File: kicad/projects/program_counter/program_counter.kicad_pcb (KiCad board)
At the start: 2 copper layers, 0 parts

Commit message: Program counter complete.
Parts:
- added C1: 0.1uF, Capacitor_THT:C_Disc_D5.0mm_W2.5mm_P5.00mm, F.Cu at (208.3, 82.8)
- added C10: 33uF, Capacitor_THT:CP_Radial_D6.3mm_P2.50mm, F.Cu at (66.0, 134.6)
- added C11: 33uF, Capacitor_THT:CP_Radial_D6.3mm_P2.50mm, F.Cu at (172.7, 116.8)
- added C12: 33uF, Capacitor_THT:CP_Radial_D6.3mm_P2.50mm, F.Cu at (152.4, 73.7)
- added C2: 0.1uF, Capacitor_THT:C_Disc_D5.0mm_W2.5mm_P5.00mm, F.Cu at (182.9, 111.8)
- added C3: 0.1uF, Capacitor_THT:C_Disc_D5.0mm_W2.5mm_P5.00mm, F.Cu at (142.2, 116.8)
- added C4: 0.1uF, Capacitor_THT:C_Disc_D5.0mm_W2.5mm_P5.00mm, F.Cu at (215.9, 111.8)
- added C5: 0.1uF, Capacitor_THT:C_Disc_D5.0mm_W2.5mm_P5.00mm, F.Cu at (114.3, 116.8)
- added C6: 0.1uF, Capacitor_THT:C_Disc_D5.0mm_W2.5mm_P5.00mm, F.Cu at (160.0, 82.8)
- added C7: 0.1uF, Capacitor_THT:C_Disc_D5.0mm_W2.5mm_P5.00mm, F.Cu at (86.4, 116.8)
- added C8: 0.1uF, Capacitor_THT:C_Disc_D5.0mm_W2.5mm_P5.00mm, F.Cu at (58.4, 116.8)
- added C9: 0.1uF, Capacitor_THT:C_Disc_D5.0mm_W2.5mm_P5.00mm, F.Cu at (124.5, 86.4)
- added D1: LED, eight-bit-computer:LED_D5.0mm_Horizontal_O3.81mm_Z3.0mm, F.Cu at (251.5, 63.5)
- added D10: LED, eight-bit-computer:LED_D5.0mm_Horizontal_O3.81mm_Z3.0mm, F.Cu at (194.3, 63.5)
- added D11: LED, eight-bit-computer:LED_D5.0mm_Horizontal_O3.81mm_Z3.0mm, F.Cu at (188.0, 63.5)
- added D12: LED, eight-bit-computer:LED_D5.0mm_Horizontal_O3.81mm_Z3.0mm, F.Cu at (181.6, 63.5)
- added D13: LED, eight-bit-computer:LED_D5.0mm_Horizontal_O3.81mm_Z3.0mm, F.Cu at (175.3, 63.5)
- added D14: LED, eight-bit-computer:LED_D5.0mm_Horizontal_O3.81mm_Z3.0mm, F.Cu at (168.9, 63.5)
- added D15: LED, eight-bit-computer:LED_D5.0mm_Horizontal_O3.81mm_Z3.0mm, F.Cu at (162.6, 63.5)
- added D16: LED, eight-bit-computer:LED_D5.0mm_Horizontal_O3.81mm_Z3.0mm, F.Cu at (156.2, 63.5)
- added D2: LED, eight-bit-computer:LED_D5.0mm_Horizontal_O3.81mm_Z3.0mm, F.Cu at (245.1, 63.5)
- added D3: LED, eight-bit-computer:LED_D5.0mm_Horizontal_O3.81mm_Z3.0mm, F.Cu at (238.8, 63.5)
- added D4: LED, eight-bit-computer:LED_D5.0mm_Horizontal_O3.81mm_Z3.0mm, F.Cu at (232.4, 63.5)
- added D5: LED, eight-bit-computer:LED_D5.0mm_Horizontal_O3.81mm_Z3.0mm, F.Cu at (226.1, 63.5)
- added D6: LED, eight-bit-computer:LED_D5.0mm_Horizontal_O3.81mm_Z3.0mm, F.Cu at (219.7, 63.5)
- added D7: LED, eight-bit-computer:LED_D5.0mm_Horizontal_O3.81mm_Z3.0mm, F.Cu at (213.4, 63.5)
- added D8: LED, eight-bit-computer:LED_D5.0mm_Horizontal_O3.81mm_Z3.0mm, F.Cu at (207.0, 63.5)
- added D9: LED, eight-bit-computer:LED_D5.0mm_Horizontal_O3.81mm_Z3.0mm, F.Cu at (200.7, 63.5)
- added J1: Conn_01x16_Female, Connector_PinSocket_2.54mm:PinSocket_1x16_P2.54mm_Horizontal, F.Cu at (91.4, 61.0)
- added J2: Control_signal_backplane, eight-bit-computer:backplane-connector-single-row-annotated, F.Cu at (251.5, 144.8)
- added J3: Bus_connection, eight-bit-computer:bus-connection, F.Cu at (147.3, 144.8)
- added J4: Aux_connection, eight-bit-computer:aux-connection, F.Cu at (96.5, 144.8)
- added RN1: R_Network08_US, Resistor_THT:R_Array_SIP9, F.Cu at (215.9, 73.7)
- added RN2: R_Network08_US, Resistor_THT:R_Array_SIP9, F.Cu at (167.6, 73.7)
- added U1: 74HCT04, Package_DIP:DIP-14_W7.62mm, F.Cu at (129.5, 88.9)
- added U2: 74HCT245, Package_DIP:DIP-20_W7.62mm, F.Cu at (213.4, 88.9)
- added U3: 74HCT161, Package_DIP:DIP-16_W7.62mm, F.Cu at (147.3, 119.4)
- added U4: 74HCT245, Package_DIP:DIP-20_W7.62mm, F.Cu at (188.0, 119.4)
- added U5: 74HCT161, Package_DIP:DIP-16_W7.62mm, F.Cu at (119.4, 119.4)
- added U6: 74HCT245, Package_DIP:DIP-20_W7.62mm, F.Cu at (221.0, 119.4)
- added U7: 74HCT161, Package_DIP:DIP-16_W7.62mm, F.Cu at (91.4, 119.4)
- added U8: 74HCT245, Package_DIP:DIP-20_W7.62mm, F.Cu at (165.1, 88.9)
- added U9: 74HCT161, Package_DIP:DIP-16_W7.62mm, F.Cu at (63.5, 119.4)
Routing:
- net VCC: track 0.00 -> 550.0 mm, vias 0 -> 26
- net /PC_IN: track 0.00 -> 235.1 mm
- net /CTNT_01: track 0.00 -> 227.2 mm, vias 0 -> 8
- net /CTNT_02: track 0.00 -> 227.2 mm, vias 0 -> 8
- net /CTNT_03: track 0.00 -> 227.2 mm, vias 0 -> 8
- net /CTNT_00: track 0.00 -> 227.0 mm, vias 0 -> 6
- net /CTNT_07: track 0.00 -> 226.8 mm, vias 0 -> 6
- net /CTNT_06: track 0.00 -> 226.1 mm, vias 0 -> 8
- net /CTNT_05: track 0.00 -> 226.1 mm, vias 0 -> 8
- net /CTNT_04: track 0.00 -> 226.1 mm, vias 0 -> 8
- net /PC_OUT: track 0.00 -> 224.4 mm
- net /CTNT_15: track 0.00 -> 214.7 mm, vias 0 -> 4
- net /CTNT_14: track 0.00 -> 213.9 mm, vias 0 -> 8
- net /CTNT_13: track 0.00 -> 213.9 mm, vias 0 -> 8
- net /CTNT_12: track 0.00 -> 213.9 mm, vias 0 -> 8
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- added copper zone on B.Cu, net GND
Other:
- board outline added: 203.2 x 97.8 mm
- board text added: "Content"
- board text added: "PROGRAM COUNTER"

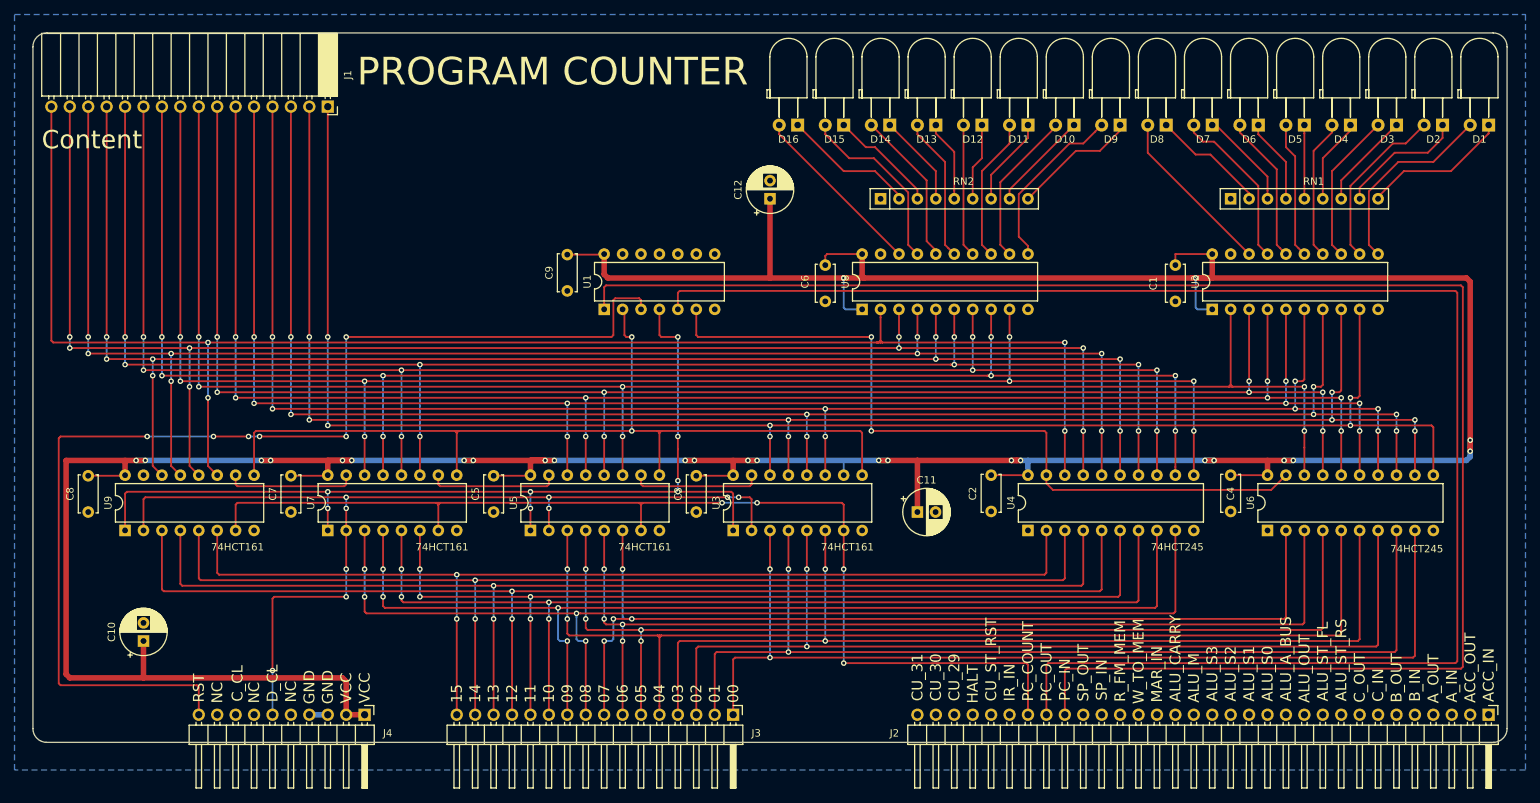
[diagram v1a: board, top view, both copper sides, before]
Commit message: Align output drivers for better PCB layout
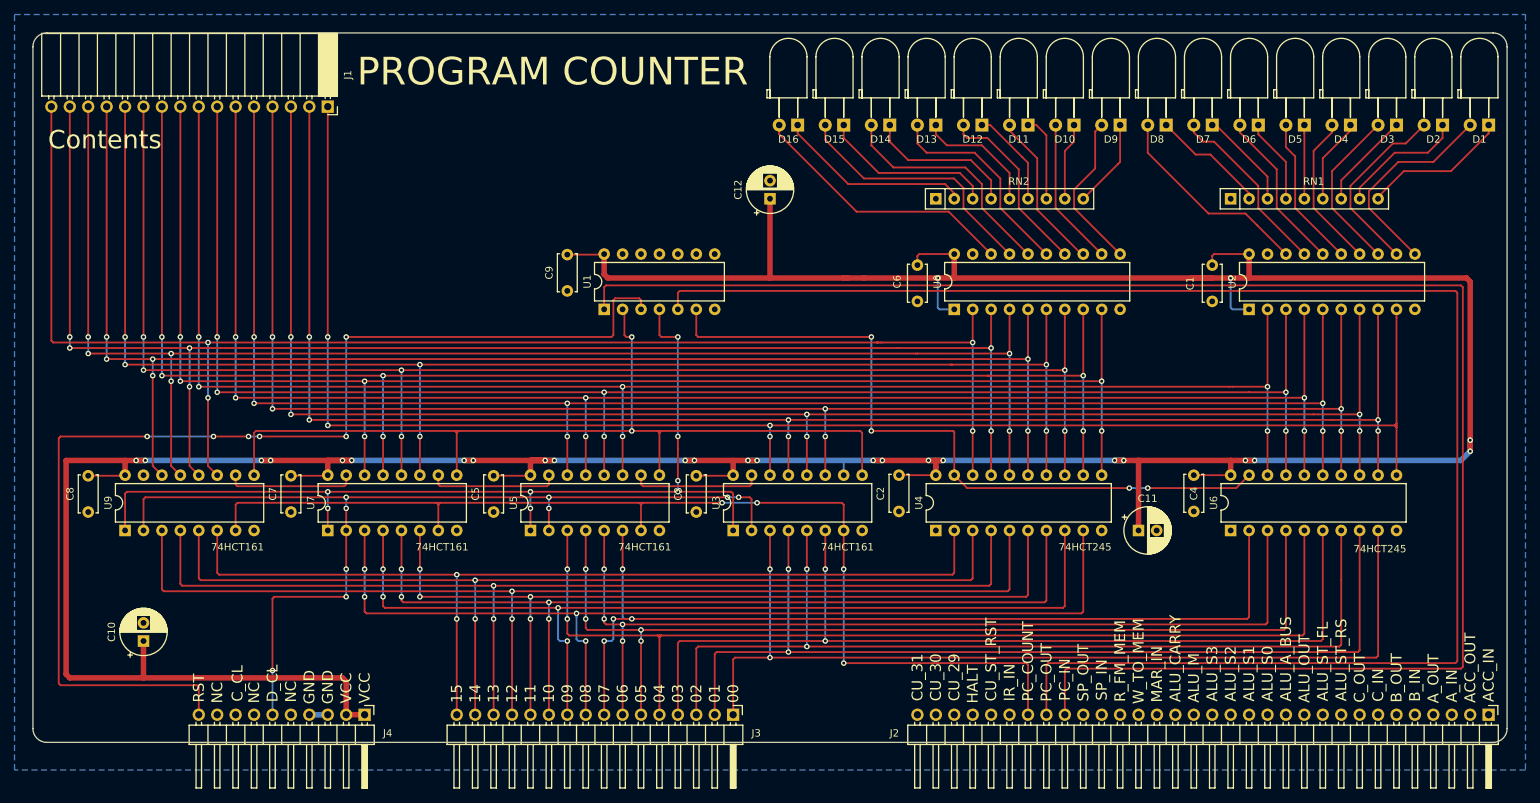
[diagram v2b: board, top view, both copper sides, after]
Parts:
- moved C11 30.6 mm to (203.2, 119.4)
- moved U4 12.7 mm to (175.3, 119.4)
- moved U8 12.7 mm to (177.8, 88.9)
- moved C2 12.7 mm to (170.2, 111.8)
- moved C6 12.7 mm to (172.7, 82.8)
- moved RN2 7.62 mm to (175.3, 73.7)
- moved C1 5.08 mm to (213.4, 82.8)
- moved C4 5.08 mm to (210.8, 111.8)
- moved U2 5.08 mm to (218.4, 88.9)
- moved U6 5.08 mm to (215.9, 119.4)
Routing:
- net /CTNT_15: track 214.7 -> 201.3 mm
- net /CTNT_10: track 213.4 -> 200.7 mm, vias 8 -> 6
- net /BUS_12: track 163.0 -> 150.3 mm
- net /CTNT_14: track 213.9 -> 201.2 mm, vias 8 -> 6
- net /CTNT_13: track 213.9 -> 201.2 mm, vias 8 -> 6
- net /CTNT_12: track 213.9 -> 201.2 mm, vias 8 -> 6
- net /CTNT_09: track 213.6 -> 200.9 mm, vias 8 -> 6
- net /BUS_11: track 130.9 -> 118.2 mm
- net /BUS_10: track 136.6 -> 123.9 mm
- net Net-(D16-Pad2): track 24.6 -> 37.3 mm
- net /CTNT_11: track 213.6 -> 200.9 mm, vias 8 -> 6
- net /CTNT_08: track 213.4 -> 200.7 mm, vias 8 -> 6
- net /BUS_15: track 145.5 -> 132.8 mm
- net /BUS_14: track 151.6 -> 138.9 mm
- net /BUS_13: track 157.2 -> 144.5 mm
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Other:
- board text added: "Contents"
- board text removed: "Content"

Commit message: Move kikad libs to sixteen bit location and update projects.
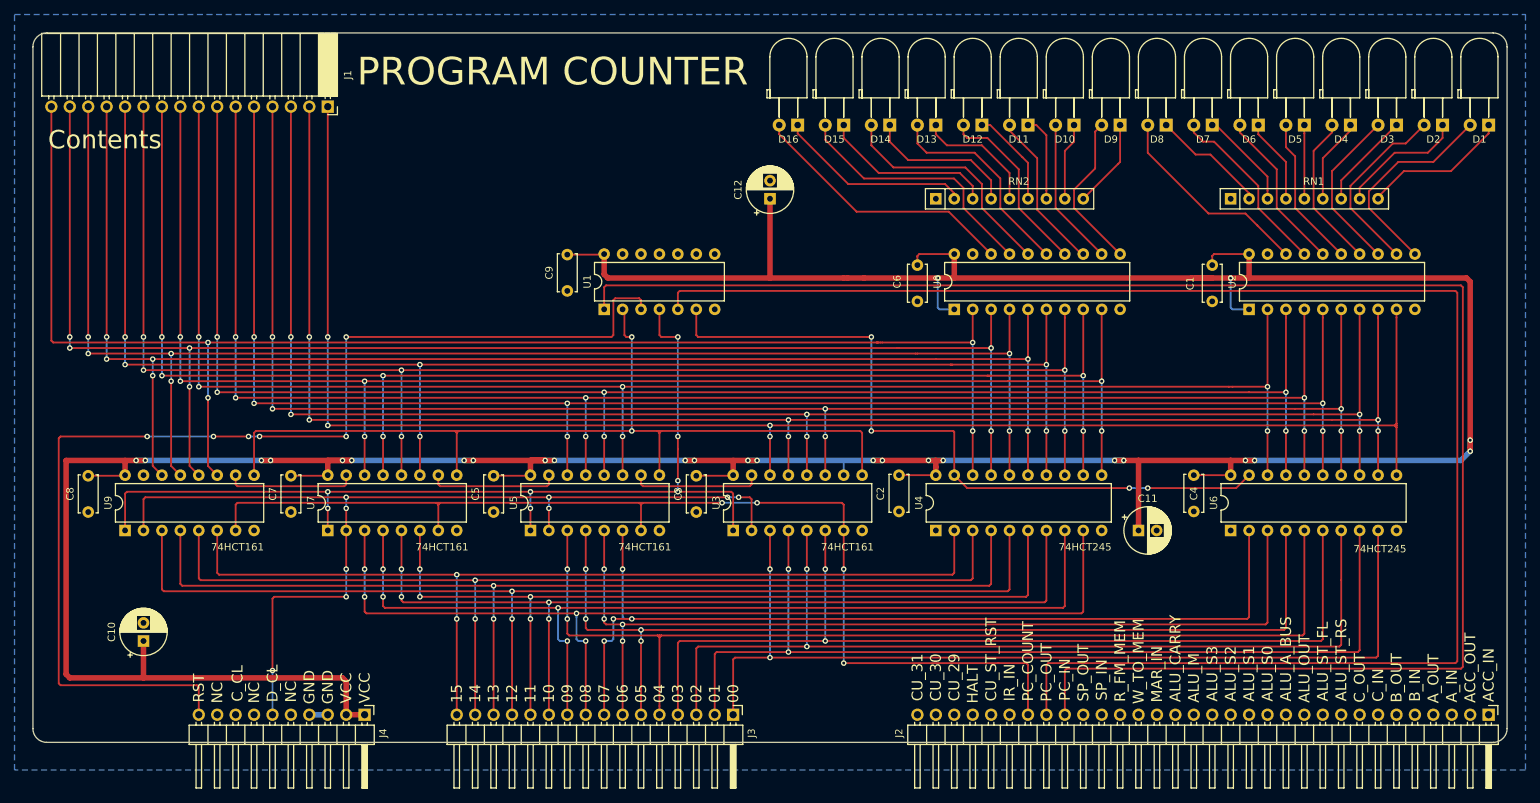
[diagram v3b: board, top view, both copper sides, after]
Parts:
- D1, D10, D11, D12, D13, D14, D15, D16, D2, D3, D4, D5, D6, D7, D8, D9: footprint eight-bit-computer:LED_D5.0mm_Horizontal_O3.81mm_Z3.0mm -> sixteen-bit-computer:LED_D5.0mm_Horizontal_O3.81mm_Z3.0mm
- J2: footprint eight-bit-computer:backplane-connector-single-row-annotated -> sixteen-bit-computer:backplane-connector-single-row-annotated
- J3: footprint eight-bit-computer:bus-connection -> sixteen-bit-computer:bus-connection
- J4: footprint eight-bit-computer:aux-connection -> sixteen-bit-computer:aux-connection

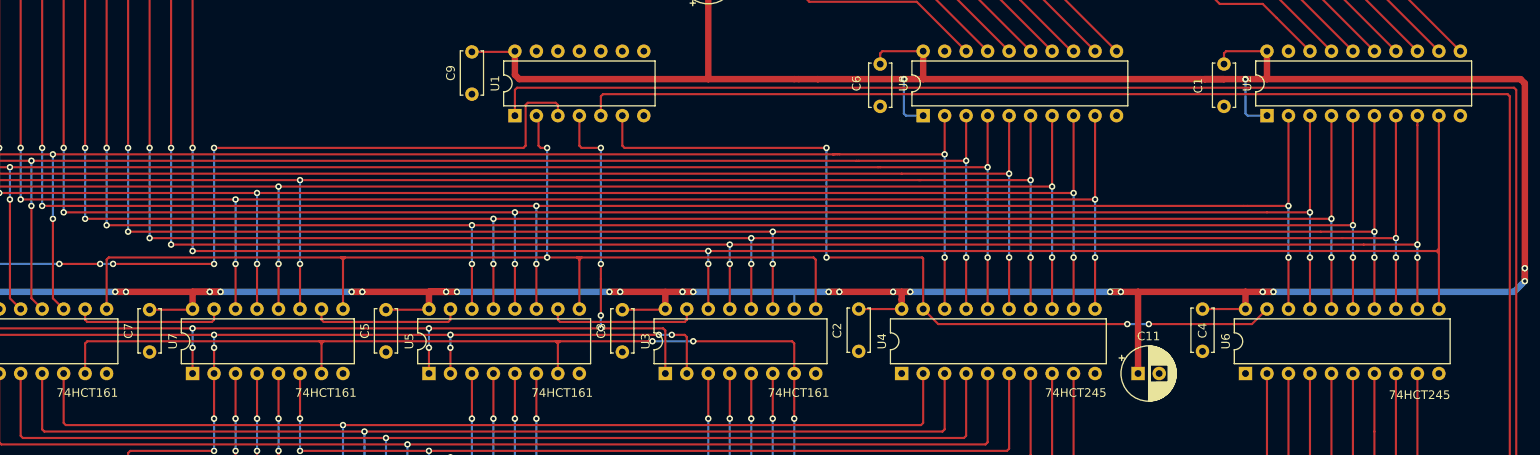
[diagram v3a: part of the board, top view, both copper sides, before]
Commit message: Switch to HC series chips and fix some labelling in program counter or register PCB.
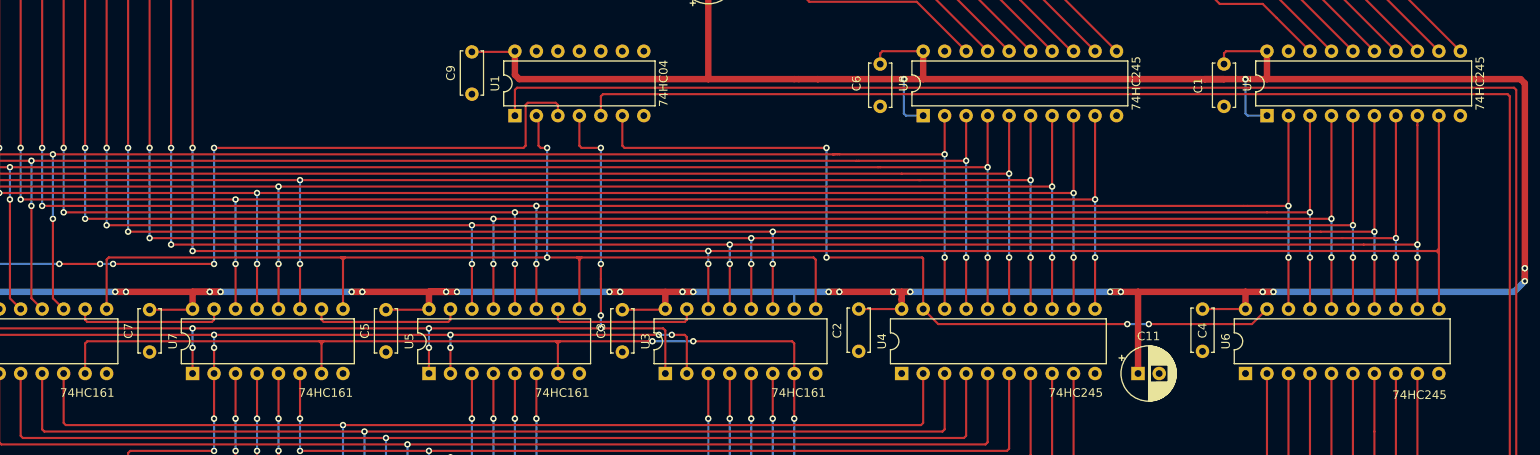
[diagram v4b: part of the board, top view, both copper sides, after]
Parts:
- U1: value 74HCT04 -> 74HC04
- U2, U4, U6, U8: value 74HCT245 -> 74HC245
- U3, U5, U7, U9: value 74HCT161 -> 74HC161
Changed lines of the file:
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@@
       (effects (font (size 1.016 1.016) (thickness 0.1778)))
     )
-    (fp_text value 74HCT161 (at -2.286 15.494 180) (layer F.SilkS)
+    (fp_text value 74HC161 (at -2.286 15.494 180) (layer F.SilkS)
       (effects (font (size 1.016 1.016) (thickness 0.1778)))
     )
@@
       (effects (font (size 1.016 1.016) (thickness 0.1778)))
     )
-    (fp_text value 74HCT245 (at 3.81 25.19 90) (layer F.Fab)
+    (fp_text value 74HC245 (at 3.81 25.19 90) (layer F.SilkS)
       (effects (font (size 1.016 1.016) (thickness 0.1778)))
     )
@@
       (effects (font (size 1.016 1.016) (thickness 0.1778)))
     )
-    (fp_text value 74HCT161 (at -2.286 15.748 180) (layer F.SilkS)
+    (fp_text value 74HC161 (at -2.286 15.748 180) (layer F.SilkS)
       (effects (font (size 1.016 1.016) (thickness 0.1778)))
     )
@@
       (effects (font (size 1.016 1.016) (thickness 0.1778)))
     )
-    (fp_text value 74HCT245 (at -2.54 20.574 180) (layer F.SilkS)
+    (fp_text value 74HC245 (at -2.54 20.574 180) (layer F.SilkS)
       (effects (font (size 1.016 1.016) (thickness 0.1778)))
     )
@@
       (effects (font (size 1.016 1.016) (thickness 0.1778)))
     )
-    (fp_text value 74HCT161 (at -2.286 15.748 180) (layer F.SilkS)
+    (fp_text value 74HC161 (at -2.286 15.748 180) (layer F.SilkS)
       (effects (font (size 1.016 1.016) (thickness 0.1778)))
     )
@@
       (effects (font (size 1.016 1.016) (thickness 0.1778)))
     )
-    (fp_text value 74HCT245 (at -2.286 20.574 180) (layer F.SilkS)
+    (fp_text value 74HC245 (at -2.286 20.574 180) (layer F.SilkS)
       (effects (font (size 1.016 1.016) (thickness 0.1778)))
     )
@@
       (effects (font (size 1.016 1.016) (thickness 0.1778)))
     )
-    (fp_text value 74HCT161 (at -2.286 15.748 180) (layer F.SilkS)
+    (fp_text value 74HC161 (at -2.286 15.748 180) (layer F.SilkS)
       (effects (font (size 1.016 1.016) (thickness 0.1778)))
     )
@@
       (effects (font (size 1.016 1.016) (thickness 0.1778)))
     )
-    (fp_text value 74HCT245 (at 3.81 25.19 90) (layer F.Fab)
+    (fp_text value 74HC245 (at 3.81 25.19 90) (layer F.SilkS)
       (effects (font (size 1.016 1.016) (thickness 0.1778)))
     )
@@
       (effects (font (size 1.016 1.016) (thickness 0.1778)))
     )
-    (fp_text value 74HCT04 (at 3.81 17.57 90) (layer F.Fab)
-      (effects (font (size 1.016 1.016) (thickness 0.1778)))
-    )
+    (fp_text value 74HC04 (at 3.81 17.57 90) (layer F.SilkS)
+      (effects (font (size 1.016 1.016) (thickness 0.1778)))
+    )
